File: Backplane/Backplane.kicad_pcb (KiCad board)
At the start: 2 copper layers, 17 parts, among them J1 Front panel, J2 System bus

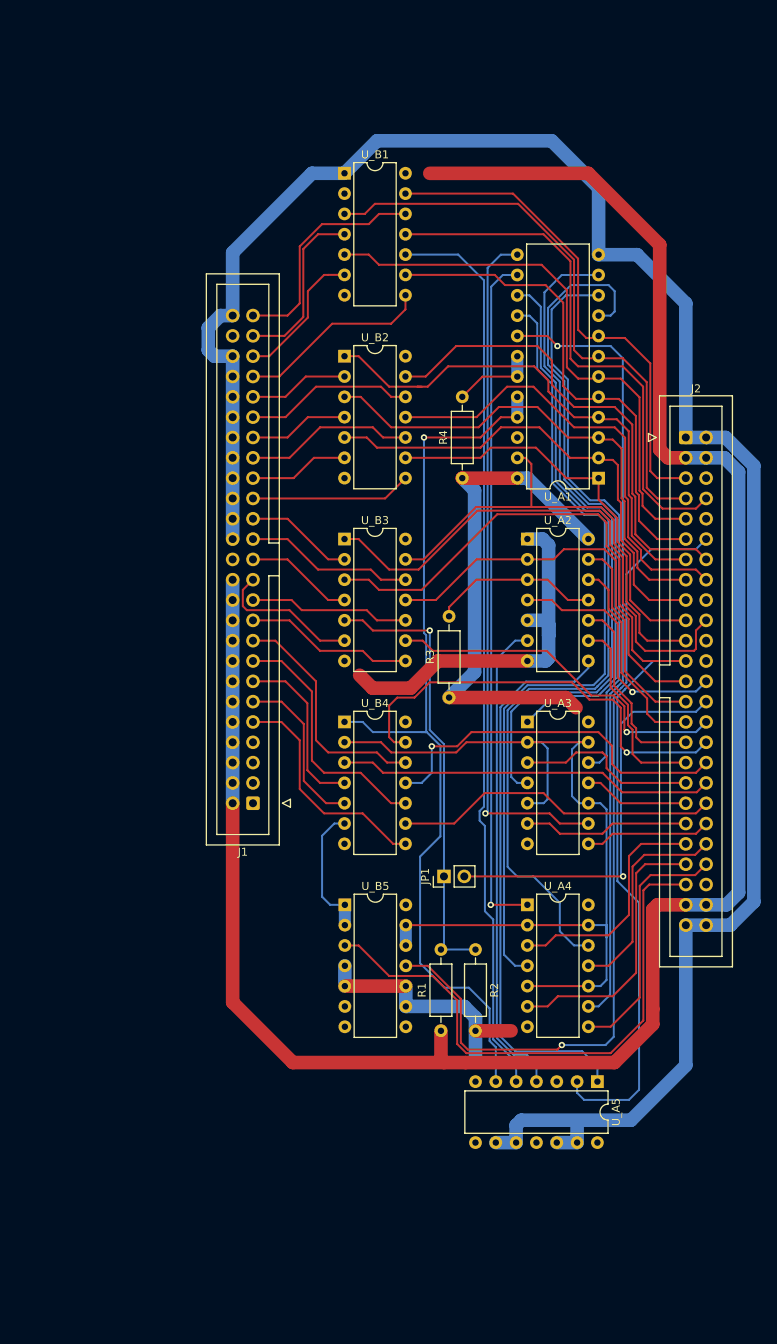
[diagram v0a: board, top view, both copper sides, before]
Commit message: Backplane: Completed
Full board layout
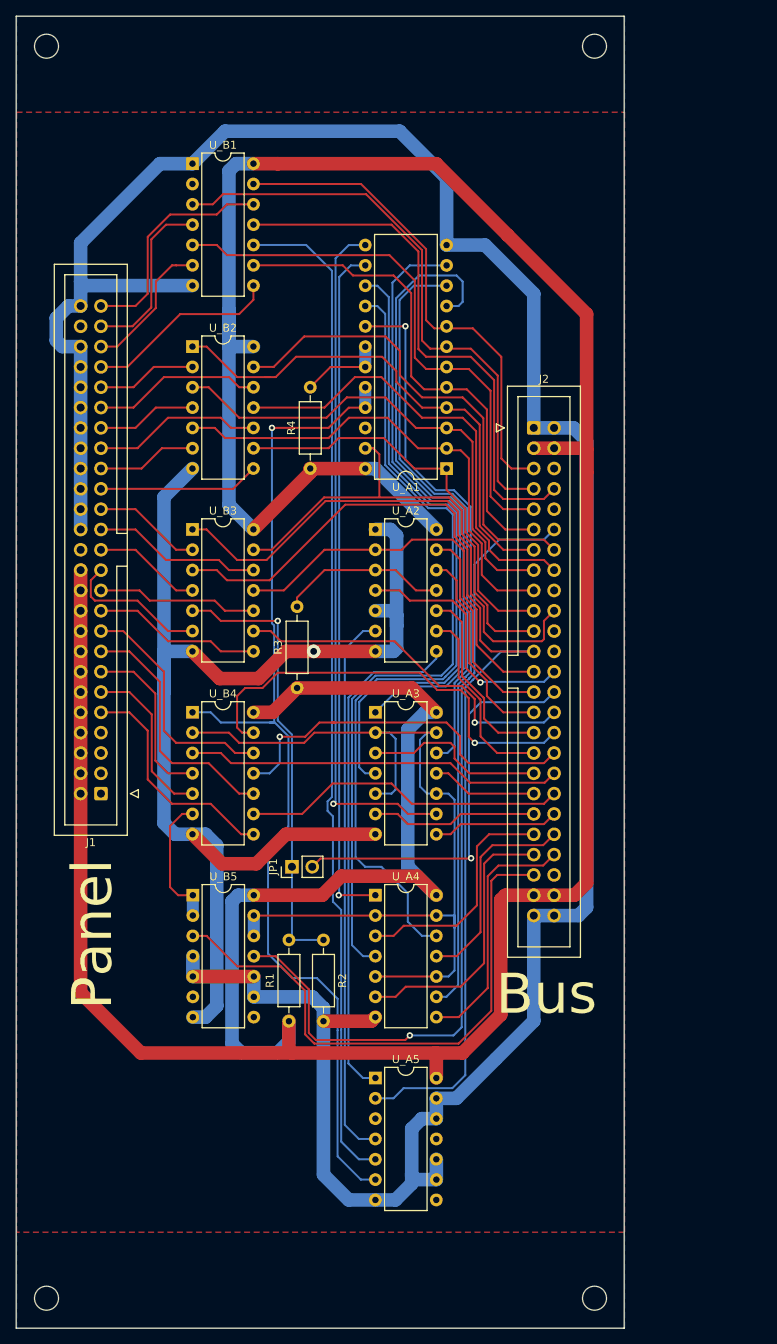
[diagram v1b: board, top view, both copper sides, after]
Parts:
- added REF**: MountingHole_3mm, MountingHole:MountingHole_3mm, F.Cu at (73.2, 181.2)
- added REF**: MountingHole_3mm, MountingHole:MountingHole_3mm, F.Cu at (141.8, 181.2)
- added REF**: MountingHole_3mm, MountingHole:MountingHole_3mm, F.Cu at (141.8, 24.8)
- added REF**: MountingHole_3mm, MountingHole:MountingHole_3mm, F.Cu at (73.2, 24.8)
- moved U_A5 27.8 mm to (114.4, 153.7), turned to 0 degrees
- moved U_A2 19.0 mm to (114.4, 85.2)
- moved U_A3 19.0 mm to (114.4, 108.0)
- moved U_A4 19.0 mm to (114.4, 130.9)
- moved J1 19.0 mm to (80.1, 118.2)
- moved J2 19.0 mm to (134.2, 72.5)
- moved JP1 19.0 mm to (103.9, 127.3)
- moved R1 19.0 mm to (103.6, 146.6)
- moved R2 19.0 mm to (107.9, 136.5)
- moved R3 19.0 mm to (104.6, 105.0)
- moved U_B1 19.0 mm to (91.5, 39.4)
- moved U_B2 19.0 mm to (91.5, 62.3)
- moved U_B3 19.0 mm to (91.5, 85.2)
- moved U_B4 19.0 mm to (91.5, 108.0)
- moved U_B5 19.0 mm to (91.5, 130.9)
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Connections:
- U_A3 pad 14: (no net) -> Vcc
- U_A3 pad 7: (no net) -> Gnd
- U_A4 pad 14: (no net) -> Vcc
- U_A4 pad 7: (no net) -> Gnd
- U_A5 pad 14: (no net) -> Vcc
- U_A5 pad 7: (no net) -> Gnd
- U_B1 pad 14: (no net) -> Vcc
- U_B1 pad 7: (no net) -> Gnd
- U_B2 pad 14: (no net) -> Vcc
- U_B2 pad 7: (no net) -> Gnd
- U_B3 pad 14: (no net) -> Vcc
- U_B3 pad 7: (no net) -> Gnd
- U_B4 pad 14: (no net) -> Vcc
- U_B4 pad 7: (no net) -> Gnd
- U_B5 pad 14: (no net) -> Vcc
- U_B5 pad 7: (no net) -> Gnd
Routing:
- net Gnd: track 337.6 -> 495.6 mm, vias 0 -> 1
- net Vcc: track 326.9 -> 468.8 mm
- net Net-(U_A1-Pad20): track 114.7 -> 130.8 mm
- net Net-(U_A5-Pad5): track 113.5 -> 126.1 mm
- net Net-(U_A2-Pad6): track 60.1 -> 68.8 mm
- net Net-(U_A2-Pad8): track 70.4 -> 63.8 mm
- net Net-(U_A1-Pad17): track 97.9 -> 96.1 mm
- net /Sys.~{PA_{14}}: track 24.6 -> 23.9 mm
- net /Sys.~{RA_{15}}: track 50.8 -> 50.2 mm
- net /Sys.~{CA_{15}}: track 24.6 -> 24.0 mm
- net /Sys.~{A_{9}}: track 133.0 -> 133.5 mm
- net /Sys.~{RDIN}: track 67.0 -> 67.5 mm
- added copper zone on B.Cu, net Gnd
- added copper zone on F.Cu, net Vcc
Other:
- board outline added: 76 x 164 mm
- board text added: "Bus"
- board text added: "Panel"

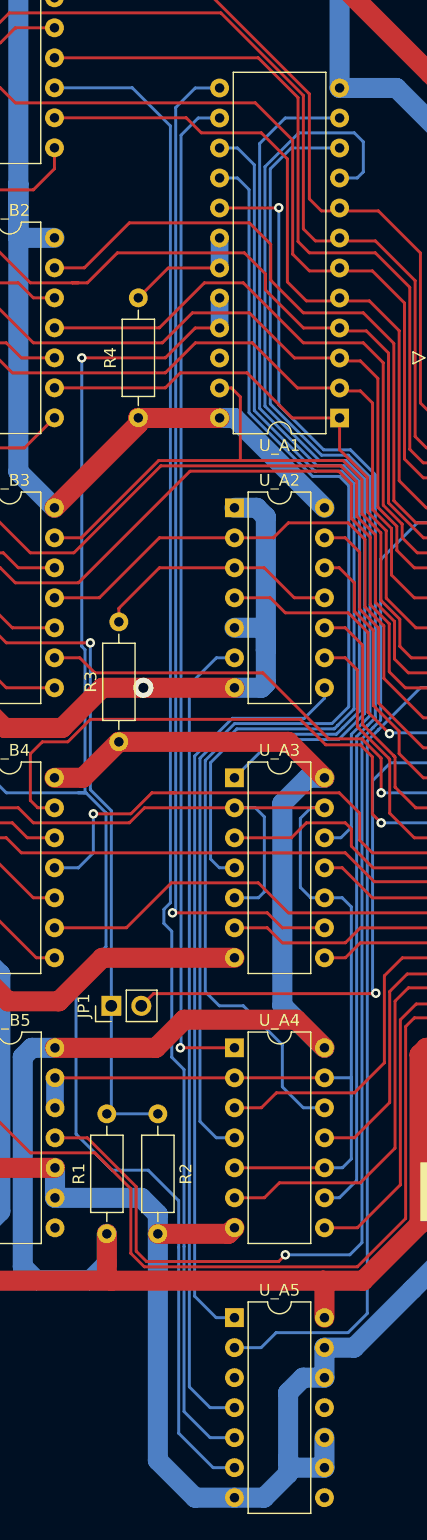
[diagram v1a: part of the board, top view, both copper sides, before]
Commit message: Backplane: Polish up
Annotate connectors on silk screen, change ROM footprint to socketed one
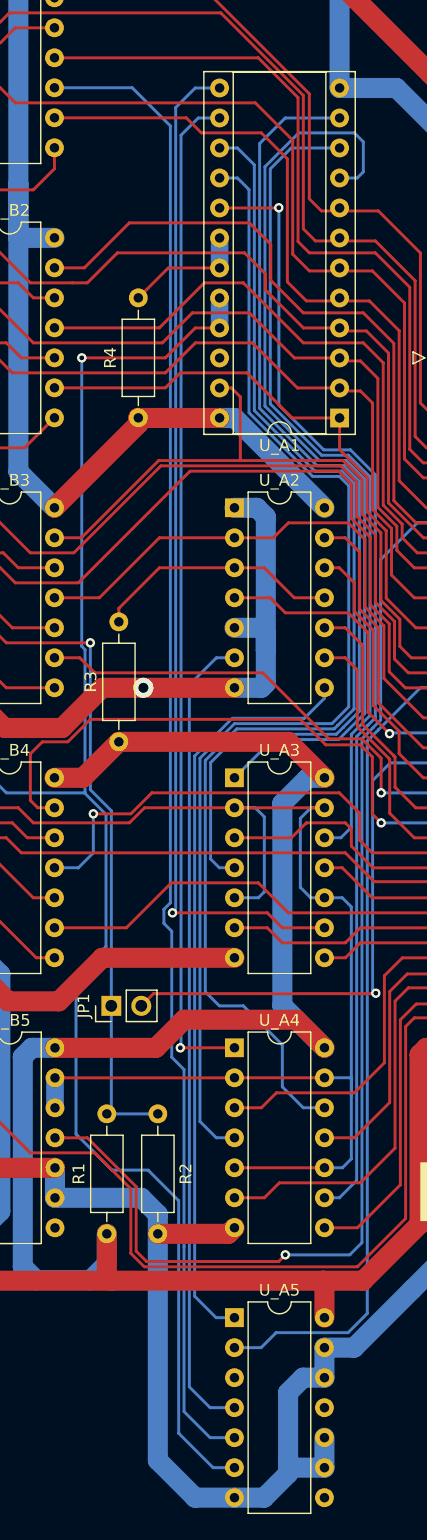
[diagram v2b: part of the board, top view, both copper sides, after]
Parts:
- U_A1: footprint Package_DIP:DIP-24_W10.16mm -> Package_DIP:DIP-24_W10.16mm_Socket
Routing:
- net Net-(U_A1-Pad20): track 130.8 -> 130.2 mm
- net /Sys.~{A_{4}}: track 63.9 -> 63.4 mm
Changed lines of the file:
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@@
     )
   )
-  (footprint "Package_DIP:DIP-24_W10.16mm" (layer "F.Cu")
+  (footprint "Package_DIP:DIP-24_W10.16mm_Socket" (layer "F.Cu")
     (at 123.257198 77.55 180)
-    (descr "24-lead though-hole mounted DIP package, row spacing 10.16 mm (400 mils)")
-    (tags "THT DIP DIL PDIP 2.54mm 10.16mm 400mil")
+    (descr "24-lead though-hole mounted DIP package, row spacing 10.16 mm (400 mils), Socket")
+    (tags "THT DIP DIL PDIP 2.54mm 10.16mm 400mil Socket")
     (property "Sheetfile" "Backplane.kicad_sch")
     (property "Sheetname" "")
@@
     )
     (fp_line (start 1.16 -1.33) (end 1.16 29.27) (layer "F.SilkS") (width 0.12))
+    (fp_line (start -1.33 29.33) (end 11.49 29.33) (layer "F.SilkS") (width 0.12))
+    (fp_line (start 9 29.27) (end 9 -1.33) (layer "F.SilkS") (width 0.12))
+    (fp_line (start 1.16 29.27) (end 9 29.27) (layer "F.SilkS") (width 0.12))
     (fp_line (start 9 -1.33) (end 6.08 -1.33) (layer "F.SilkS") (width 0.12))
+    (fp_line (start 11.49 29.33) (end 11.49 -1.39) (layer "F.SilkS") (width 0.12))
+    (fp_line (start -1.33 -1.39) (end -1.33 29.33) (layer "F.SilkS") (width 0.12))
+    (fp_line (start 11.49 -1.39) (end -1.33 -1.39) (layer "F.SilkS") (width 0.12))
     (fp_line (start 4.08 -1.33) (end 1.16 -1.33) (layer "F.SilkS") (width 0.12))
-    (fp_line (start 1.16 29.27) (end 9 29.27) (layer "F.SilkS") (width 0.12))
-    (fp_line (start 9 29.27) (end 9 -1.33) (layer "F.SilkS") (width 0.12))
     (fp_arc (start 6.08 -1.33) (mid 5.08 -0.33) (end 4.08 -1.33) (layer "F.SilkS") (width 0.12))
-    (fp_line (start 11.25 29.5) (end 11.25 -1.55) (layer "F.CrtYd") (width 0.05))
-    (fp_line (start -1.05 29.5) (end 11.25 29.5) (layer "F.CrtYd") (width 0.05))
-    (fp_line (start 11.25 -1.55) (end -1.05 -1.55) (layer "F.CrtYd") (width 0.05))
-    (fp_line (start -1.05 -1.55) (end -1.05 29.5) (layer "F.CrtYd") (width 0.05))
+    (fp_line (start -1.55 -1.6) (end -1.55 29.55) (layer "F.CrtYd") (width 0.05))
+    (fp_line (start 11.7 29.55) (end 11.7 -1.6) (layer "F.CrtYd") (width 0.05))
+    (fp_line (start -1.55 29.55) (end 11.7 29.55) (layer "F.CrtYd") (width 0.05))
+    (fp_line (start 11.7 -1.6) (end -1.55 -1.6) (layer "F.CrtYd") (width 0.05))
     (fp_line (start 0.51 29.21) (end 0.51 -0.27) (layer "F.Fab") (width 0.1))
+    (fp_line (start 11.43 -1.33) (end -1.27 -1.33) (layer "F.Fab") (width 0.1))
+    (fp_line (start 11.43 29.27) (end 11.43 -1.33) (layer "F.Fab") (width 0.1))
+    (fp_line (start 9.65 29.21) (end 0.51 29.21) (layer "F.Fab") (width 0.1))
+    (fp_line (start 0.51 -0.27) (end 1.51 -1.27) (layer "F.Fab") (width 0.1))
+    (fp_line (start 9.65 -1.27) (end 9.65 29.21) (layer "F.Fab") (width 0.1))
+    (fp_line (start -1.27 -1.33) (end -1.27 29.27) (layer "F.Fab") (width 0.1))
     (fp_line (start 1.51 -1.27) (end 9.65 -1.27) (layer "F.Fab") (width 0.1))
-    (fp_line (start 0.51 -0.27) (end 1.51 -1.27) (layer "F.Fab") (width 0.1))
-    (fp_line (start 9.65 29.21) (end 0.51 29.21) (layer "F.Fab") (width 0.1))
-    (fp_line (start 9.65 -1.27) (end 9.65 29.21) (layer "F.Fab") (width 0.1))
+    (fp_line (start -1.27 29.27) (end 11.43 29.27) (layer "F.Fab") (width 0.1))
     (pad "1" thru_hole rect (at 0 0 180) (size 1.6 1.6) (drill 0.8) (layers *.Cu *.Mask)
       (net 4 "/Sys.~{A_{7}}") (pinfunction "A7") (pintype "input"))
@@
     (pad "24" thru_hole oval (at 10.16 0 180) (size 1.6 1.6) (drill 0.8) (layers *.Cu *.Mask)
       (net 92 "Vcc") (pinfunction "VCC") (pintype "power_in"))
-    (model "${KICAD6_3DMODEL_DIR}/Package_DIP.3dshapes/DIP-24_W10.16mm.wrl"
+    (model "${KICAD6_3DMODEL_DIR}/Package_DIP.3dshapes/DIP-24_W10.16mm_Socket.wrl"
       (offset (xyz 0 0 0))
       (scale (xyz 1 1 1))
@@
   (segment (start 117.268198 66.999) (end 116.981198 66.712) (width 0.25) (layer "F.Cu") (net 7))
   (segment (start 127.403198 72.054) (end 127.403198 84.742832) (width 0.25) (layer "F.Cu") (net 7))
-  (segment (start 100.631198 66.11) (end 101.139198 66.11) (width 0.25) (layer "F.Cu") (net 7))
   (segment (start 101.901198 66.11) (end 100.631198 66.11) (width 0.25) (layer "F.Cu") (net 7))
   (segment (start 104.441198 63.57) (end 101.901198 66.11) (width 0.25) (layer "F.Cu") (net 7))
@@
   (segment (start 101.705198 109.232) (end 101.647198 109.29) (width 0.25) (layer "B.Cu") (net 20))
   (segment (start 101.647198 109.29) (end 95.043198 109.29) (width 0.25) (layer "B.Cu") (net 20))
-  (segment (start 112.549198 166.4255) (end 114.357198 166.4255) (width 0.25) (layer "B.Cu") (net 20))
-  (segment (start 109.637198 147.7655) (end 109.637198 163.5135) (width 0.25) (layer "B.Cu") (net 20))
   (segment (start 113.097198 67.39) (end 113.097198 69.93) (width 1.5) (layer "B.Cu") (net 20))
-  (segment (start 103.483198 122.311604) (end 103.483198 110.988299) (width 0.25) (layer "B.Cu") (net 20))
-  (segment (start 104.000802 141.236) (end 100.943198 138.178396) (width 0.25) (layer "B.Cu") (net 20))
-  (segment (start 103.483198 110.988299) (end 101.786295 109.291396) (width 0.25) (layer "B.Cu") (net 20))
+  (segment (start 100.943198 124.851604) (end 103.483198 122.311604) (width 0.25) (layer "B.Cu") (net 20))
+  (segment (start 103.483198 122.311604) (end 103.483198 111.116695) (width 0.25) (layer "B.Cu") (net 20))
+  (segment (start 109.637198 143.824396) (end 107.048802 141.236) (width 0.25) (layer "B.Cu") (net 20))
+  (segment (start 100.943198 138.178396) (end 100.943198 124.851604) (width 0.25) (layer "B.Cu") (net 20))
   (segment (start 101.430198 96.890305) (end 101.705198 97.165305) (width 0.25) (layer "B.Cu") (net 20))
   (segment (start 101.705198 97.165305) (end 101.705198 109.232) (width 0.25) (layer "B.Cu") (net 20))
-  (segment (start 101.786295 109.291396) (end 101.139198 109.291396) (width 0.25) (layer "B.Cu") (net 20))
-  (segment (start 109.637198 147.7655) (end 109.637198 143.824396) (width 0.25) (layer "B.Cu") (net 20))
+  (segment (start 103.483198 111.116695) (end 101.657899 109.291396) (width 0.25) (layer "B.Cu") (net 20))
+  (segment (start 112.549198 166.4255) (end 109.637198 163.5135) (width 0.25) (layer "B.Cu") (net 20))
+  (segment (start 114.357198 166.4255) (end 112.549198 166.4255) (width 0.25) (layer "B.Cu") (net 20))
+  (segment (start 104.000802 141.236) (end 100.943198 138.178396) (width 0.25) (layer "B.Cu") (net 20))
   (segment (start 101.430698 72.46) (end 101.430198 72.4605) (width 0.25) (layer "B.Cu") (net 20))
+  (segment (start 107.048802 141.236) (end 104.000802 141.236) (width 0.25) (layer "B.Cu") (net 20))
   (segment (start 93.768198 108.015) (end 91.497198 108.015) (width 0.25) (layer "B.Cu") (net 20))
-  (segment (start 100.943198 138.178396) (end 100.943198 124.851604) (width 0.25) (layer "B.Cu") (net 20))
-  (segment (start 107.048802 141.236) (end 104.000802 141.236) (width 0.25) (layer "B.Cu") (net 20))
-  (segment (start 109.637198 163.5135) (end 112.549198 166.4255) (width 0.25) (layer "B.Cu") (net 20))
-  (segment (start 100.943198 124.851604) (end 103.483198 122.311604) (width 0.25) (layer "B.Cu") (net 20))
+  (segment (start 109.637198 163.5135) (end 109.637198 143.824396) (width 0.25) (layer "B.Cu") (net 20))
   (segment (start 95.043198 109.29) (end 93.768198 108.015) (width 0.25) (layer "B.Cu") (net 20))
   (segment (start 101.430198 72.4605) (end 101.430198 96.890305) (width 0.25) (layer "B.Cu") (net 20))
-  (segment (start 109.637198 143.824396) (end 107.048802 141.236) (width 0.25) (layer "B.Cu") (net 20))
   (segment (start 99.117198 87.695) (end 101.398198 87.695) (width 0.25) (layer "F.Cu") (net 21))
   (segment (start 101.398198 87.695) (end 107.939198 81.154) (width 0.25) (layer "F.Cu") (net 21))
@@
   (segment (start 102.409198 111.068) (end 105.585594 111.068) (width 0.25) (layer "F.Cu") (net 65))
   (segment (start 124.957198 113.296) (end 124.957198 111.01) (width 0.25) (layer "F.Cu") (net 65))
-  (segment (start 109.267198 109.29) (end 108.887594 109.29) (width 0.25) (layer "F.Cu") (net 65))
   (segment (start 135.429198 114.37) (end 126.031198 114.37) (width 0.25) (layer "F.Cu") (net 65))
   (segment (start 107.363594 109.29) (end 109.267198 109.29) (width 0.25) (layer "F.Cu") (net 65))

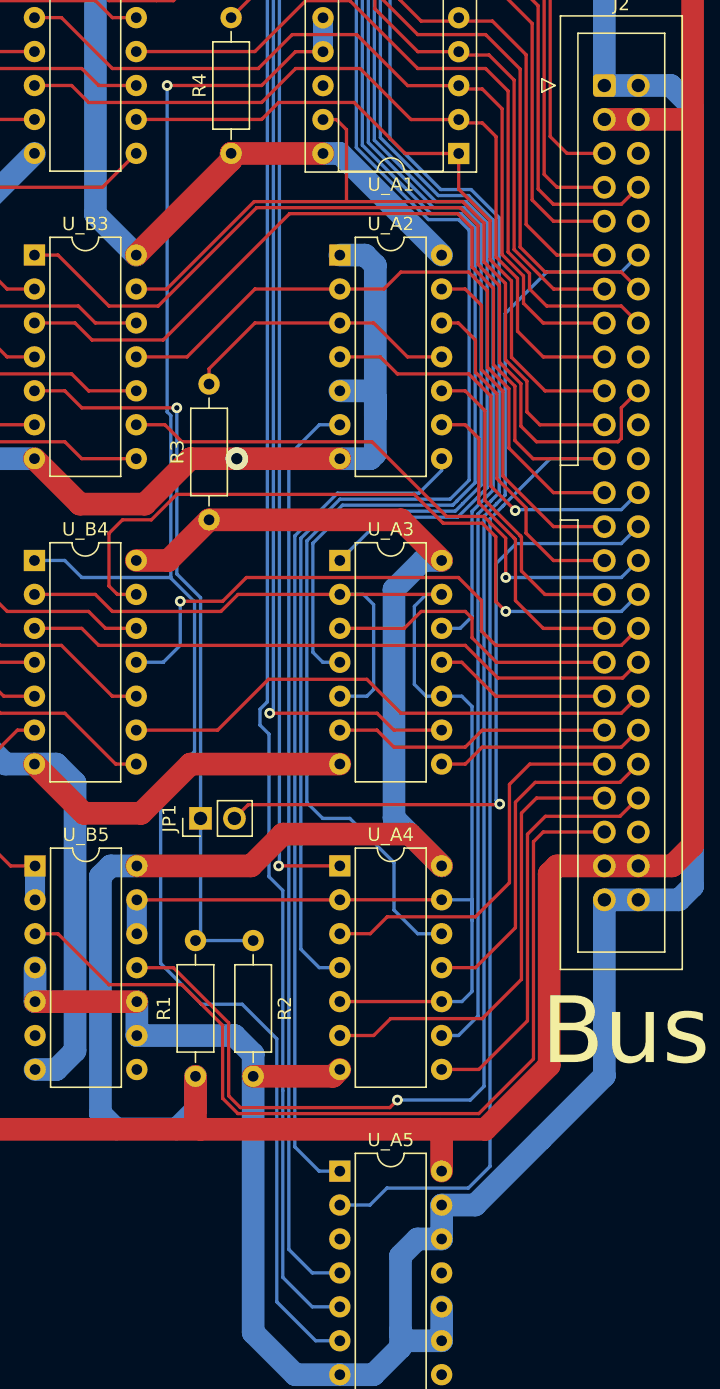
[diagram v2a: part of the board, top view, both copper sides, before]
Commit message: Backplane: Improve flooding
Move some vias around to fill more area
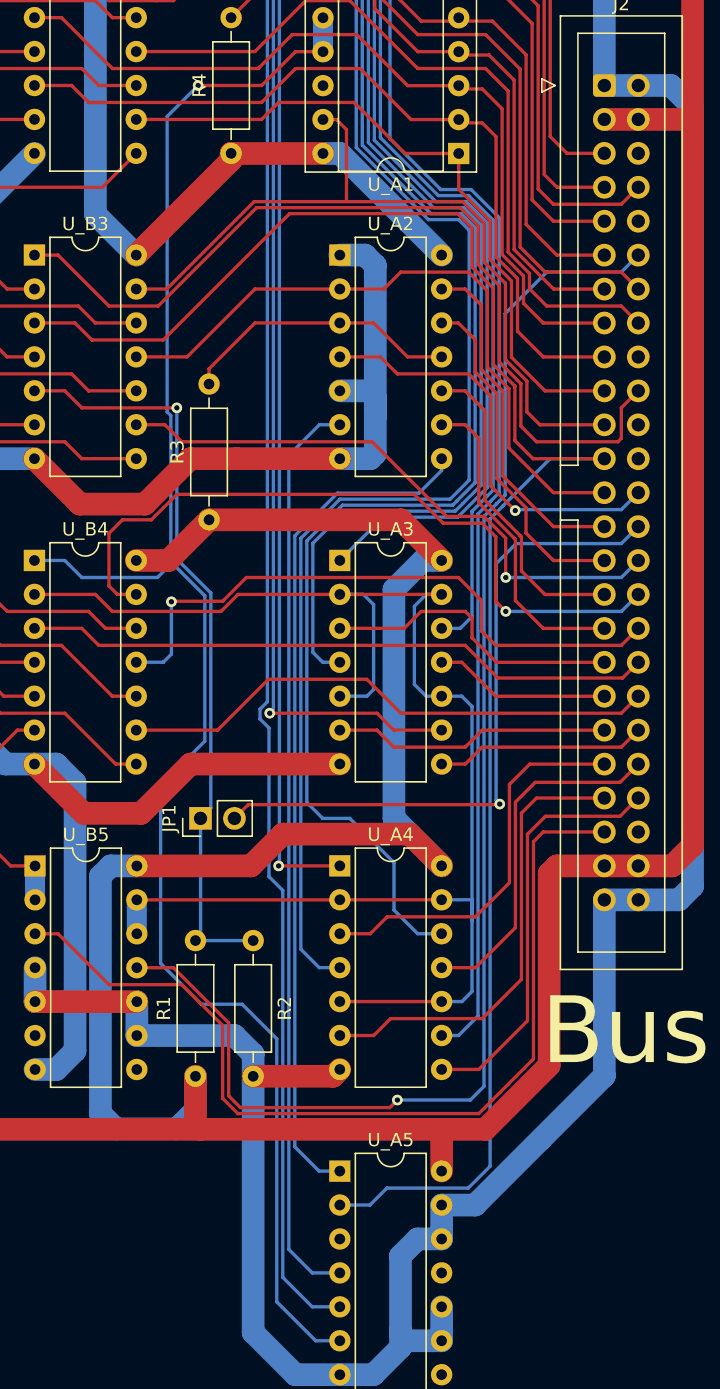
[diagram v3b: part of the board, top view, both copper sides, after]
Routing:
- net Net-(JP1-Pad1): track 56.3 -> 56.9 mm
- net Gnd: vias 1 -> 0
